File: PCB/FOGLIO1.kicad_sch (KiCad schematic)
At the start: 76 parts, among them J2 USB_C_Receptacle_PowerOnly_6P, J3 6871XX182122_687110182122, J5 Conn_01x03_Pin, J7 Conn_02x06_Odd_Even, U1 TPD2E2U06DCK, U2 ADS131M08xPBS, U3 74LVC1G17, U4 LM27762, U7 LP5907MFX-3.3

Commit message: Re-pin J7 (MCU header) to match U2's digital pin order
The clock and the six ADC digital lines enter U2 (ADS131M08) from its
right side. From top to bottom they arrive as CLKIN (via U3/R80), DIN,
DOUT (via R81), SCLK, DRDY (via R82) and CS, with SYNC at the bottom
corner. With the old J7 order the F.Cu fan-out to the header crossed
itself. Moving digital lines to B.Cu is not an option, because B.Cu
sits over the +2V5 analog plane.

The new order lets the lines run up the right board edge and enter J7
from the side:
- DIN, MISO, SCLK, DRDY and CS go through the 1.9 mm gap between the
  two pad rows. They peel off down into the bottom row or up into the
  top row in the order they arrive.
- SYNC reaches pad 1 from the side.
- MCU_CLK stays on pin 2, directly above U3.

  pin  before           after
   1   GND              ADC_SYNC_RESET
   4   ADC_SCLK         ADC_MOSI
   5   ADC_MOSI         ADC_CS
   7   ADC_MISO         GND
   8   ADC_CS           ADC_MISO
  10   ADC_SYNC_RESET   ADC_SCLK
  (2 MCU_CLK, 3/6/11/12 GND and 9 ADC_DRDY unchanged)

- There are still 5 GND pins. MCU_CLK keeps GND on pin 3 as its
  ribbon-cable neighbour; its other neighbour, pin 1, is SYNC_RESET,
  which rarely switches.
- The MCU-side wiring must follow this table (CHANGELOG Part 8).

Schematic (FOGLIO1):
- Pin 1's tie to pin 3's GND is removed (wire and junction). Pin 3
  keeps its own GND symbol (#PWR0160 moved), and pin 1 gets an
  ADC_SYNC_RESET label.
- Pin 7's ADC_MISO label is replaced by a GND symbol (#PWR0243, new).
- The other labels are renamed in place.
- Netlist: only J7's pin memberships change. ERC: 0 errors, with the
  same 31 warnings as before.

PCB:
- The J7 pad nets are updated to match, so Update PCB from Schematic
  has nothing to change.
- Pin 1's GND stub and via are removed. Pin 7 gets a GND stub and a via
  past its outer end at (163.76, 82.43).
- DRC: identical to the previous commit.

Co-Authored-By: Claude Opus 5.5 <noreply@anthropic.com>
Claude-Session: http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
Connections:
- net ADC_CS: now also J7.5 (Pin_5); no longer J7.8 (Pin_8)
- net ADC_MISO: now also J7.8 (Pin_8); no longer J7.7 (Pin_7)
- net ADC_MOSI: now also J7.4 (Pin_4); no longer J7.5 (Pin_5)
- net ADC_SCLK: now also J7.10 (Pin_10); no longer J7.4 (Pin_4)
- net ADC_SYNC_RESET: now also J7.1 (Pin_1); no longer J7.10 (Pin_10)
- net GND: now also J7.7 (Pin_7); no longer J7.1 (Pin_1)
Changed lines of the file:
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@@
 	)
 	(junction
-		(at 228.6 127)
-		(diameter 0)
-		(color 0 0 0 0)
-	)
-	(junction
 		(at 125.73 62.23)
 		(diameter 0)
@@
 	(wire
 		(pts
-			(xy 231.14 129.54) (xy 228.6 129.54)
+			(xy 231.14 129.54) (xy 226.06 129.54)
 		)
 		(stroke
@@
 	(wire
 		(pts
-			(xy 228.6 127) (xy 228.6 129.54)
-		)
-		(stroke
-			(width 0)
-			(type default)
-		)
-	)
-	(wire
-		(pts
 			(xy 340.36 203.2) (xy 340.36 205.74)
 		)
@@
 		)
 	)
-	(label "ADC_CS"
+	(label "ADC_MISO"
 		(at 248.92 134.62 0)
 		(effects
@@
 		)
 	)
-	(label "ADC_SYNC_RESET"
+	(label "ADC_SCLK"
 		(at 248.92 137.16 0)
 		(effects
@@
 		)
 	)
-	(label "ADC_MISO"
-		(at 226.06 134.62 180)
-		(effects
-			(font
-				(size 1.27 1.27)
-			)
-			(justify right bottom)
-		)
-	)
 	(label "AIN3P"
 		(at 114.3 142.24 180)
@@
 		)
 	)
-	(label "ADC_MOSI"
+	(label "ADC_CS"
 		(at 226.06 132.08 180)
 		(effects
@@
 		)
 	)
-	(label "ADC_SCLK"
+	(label "ADC_MOSI"
 		(at 248.92 129.54 0)
 		(effects
@@
 		)
 	)
+	(label "ADC_SYNC_RESET"
+		(at 226.06 127 180)
+		(effects
+			(font
+				(size 1.27 1.27)
+			)
+			(justify right bottom)
+		)
+	)
 	(hierarchical_label "Vout1"
 		(shape input)
@@
 	(symbol
 		(lib_id "power:GND")
-		(at 226.06 127 270)
+		(at 226.06 129.54 270)
 		(unit 1)
 		(body_style 1)
@@
 		)
 		(property "Footprint" ""
-			(at 226.06 127 0)
+			(at 226.06 129.54 0)
 			(hide yes)
 			(show_name no)
@@
 		)
 		(property "Datasheet" ""
-			(at 226.06 127 0)
+			(at 226.06 129.54 0)
 			(hide yes)
 			(show_name no)
@@
 		)
 		(property "Description" "Power symbol creates a global label with name \"GND\""
-			(at 226.06 127 0)
+			(at 226.06 129.54 0)
 			(hide yes)
 			(show_name no)
@@
 					(unit 1)
 				)
+			)
+		)
+	)
+	(symbol
+		(lib_id "power:GND")
+		(at 226.06 134.62 270)
+		(unit 1)
+		(body_style 1)
+		(exclude_from_sim no)
+		(in_bom yes)
+		(on_board yes)
+		(in_pos_files yes)
+		(dnp no)
+		(property "Reference" "#PWR0243"
+			(at 226.06 143.51 0)
+			(hide yes)
+			(show_name no)
+			(do_not_autoplace no)
+			(effects
+				(font
+					(size 1.27 1.27)
+				)
+			)
+		)
+		(property "Value" "GND"
+			(at 226.06 143.51 0)
+			(hide yes)
+			(show_name no)
+			(do_not_autoplace no)
+			(effects
+				(font
+					(size 1.27 1.27)
+				)
+			)
+		)
+		(property "Footprint" ""
+			(at 226.06 134.62 0)
+			(hide yes)
+			(show_name no)
+			(do_not_autoplace no)
+			(effects
+				(font
+					(size 1.27 1.27)
+				)
+			)
+		)
+		(property "Datasheet" ""
+			(at 226.06 134.62 0)
+			(hide yes)
+			(show_name no)
+			(do_not_autoplace no)
+			(effects
+				(font
+					(size 1.27 1.27)
+				)
+			)
+		)
+		(property "Description" "Power symbol creates a global label with name \"GND\""
+			(at 226.06 134.62 0)
+			(hide yes)
+			(show_name no)
+			(do_not_autoplace no)
+			(effects
+				(font
+					(size 1.27 1.27)
+				)
+			)
+		)
+		(pin "1"
+		)
+		(instances
+			(project "PCB v2"
+				(path "/24ef9d1c-01f2-41da-ba56-668788d745bf/5688e730-73cf-4d97-bb68-8c6c1c24aa96"
+					(reference "#PWR0243")
+					(unit 1)
+				)

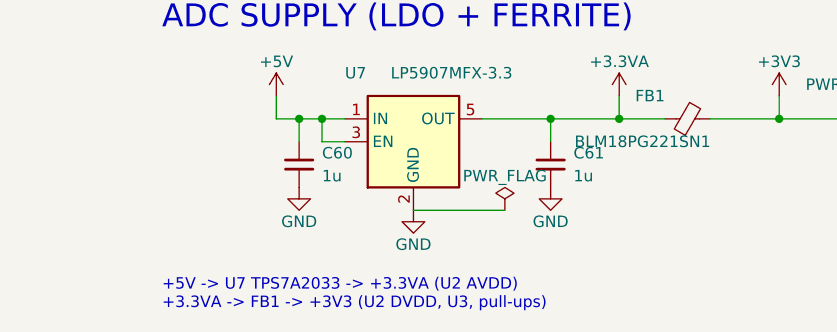
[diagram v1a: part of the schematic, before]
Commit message: Schematic: correct the U7 regulator named in the power note
The FOGLIO1 power-tree note still said "+5V -> U7 TPS7A2033 ->
+3.3VA". U7 was changed to LP5907MFX-3.3/NOPB, which has the same
SOT-23-5 pinout and footprint; the TPS7A2033 was out of stock with a
26-week lead. The symbol, value, MPN and BOM already name the LP5907;
only this text note was stale.

The note now reads "+5V -> U7 LP5907MFX-3.3 -> +3.3VA (U2 AVDD)".
Text-only change; ERC: 0 errors.

Co-Authored-By: Claude Opus 5.5 <noreply@anthropic.com>
Claude-Session: https://claude.ai/code/session_01TYMP7BCHvS3DvLnCv8UeQA
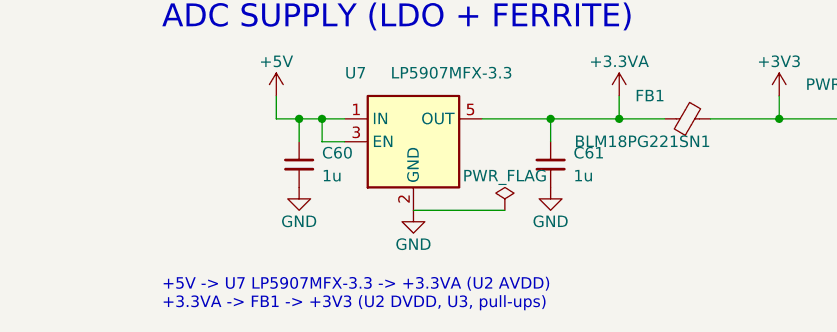
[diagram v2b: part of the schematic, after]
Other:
- note added: "+5V -> U7 LP5907MFX-3.3 -> +3.3VA (U2 AVDD) +3.3VA -> FB1 -> +3V3 (U2 DVDD, U3, pull-ups)"
- note removed: "+5V -> U7 TPS7A2033 -> +3.3VA (U2 AVDD) +3.3VA -> FB1 -> +3V3 (U2 DVDD, U3, pull-ups)"
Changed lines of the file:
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@@
 		)
 	)
-	(text "+5V -> U7 TPS7A2033 -> +3.3VA (U2 AVDD)\n+3.3VA -> FB1 -> +3V3 (U2 DVDD, U3, pull-ups)"
+	(text "+5V -> U7 LP5907MFX-3.3 -> +3.3VA (U2 AVDD)\n+3.3VA -> FB1 -> +3V3 (U2 DVDD, U3, pull-ups)"
 		(exclude_from_sim no)
 		(at 297.18 220.98 0)
